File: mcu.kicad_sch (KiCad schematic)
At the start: 49 parts, among them J1 JTAG, J4 BOOT0, J5 Debug, SW1 ~{RST}, SW2 Config, U1 STM32H573VITx, U10 IS66WVS8M8FBLL-104NL, Y1 25MHz

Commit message: drawings: added title and project name
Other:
- company: (none) -> github.com/gabbla
- title: (none) -> MCU
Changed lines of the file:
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@@
 	(generator_version "8.0")
 	(paper "A3")
+	(title_block
+		(title "MCU")
+		(rev "v0.1.0")
+		(company "github.com/gabbla")
+		(comment 1 "${PROJECTNAME}")
+	)

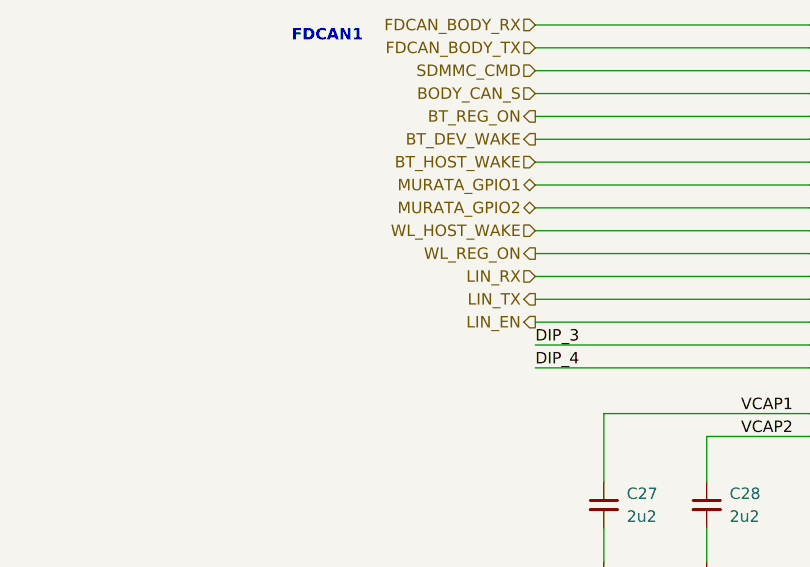
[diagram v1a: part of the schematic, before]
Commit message: sch: added UART4 note on LIN
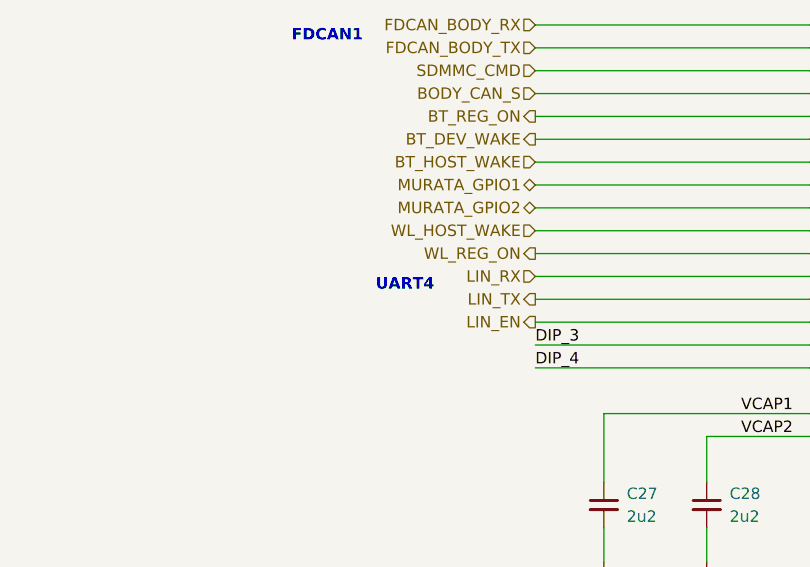
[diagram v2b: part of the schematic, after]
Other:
- note added: "UART4"

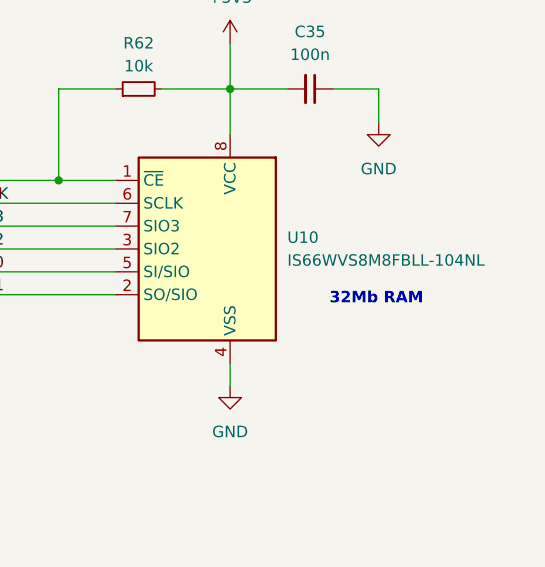
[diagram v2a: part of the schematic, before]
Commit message: External RAM changed to APS6404L 64Mbit
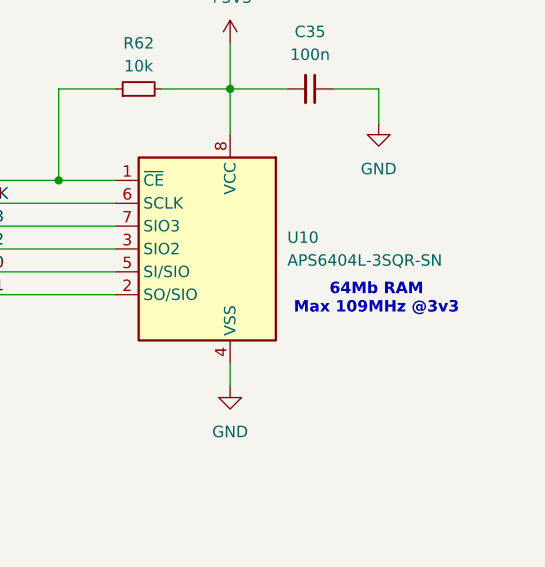
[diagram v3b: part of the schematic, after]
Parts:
- U10: value IS66WVS8M8FBLL-104NL -> APS6404L-3SQR-SN
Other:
- note added: "64Mb RAM Max 109MHz @3v3"
- note removed: "32Mb RAM"

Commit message: io, spi flash, stuff
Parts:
- added C24, C25: 100n, Capacitor_SMD:C_0603_1608Metric_Pad1.08x0.95mm_HandSolder, symbol Device:C_Small
- added R25, R26, R27: 4k7, Resistor_SMD:R_0603_1608Metric_Pad0.98x0.95mm_HandSolder, symbol Device:R_Small
- added R28: 10k, Resistor_SMD:R_0603_1608Metric_Pad0.98x0.95mm_HandSolder, symbol Device:R_Small
- added U3: PCA9557PW, Package_SO:TSSOP-16_4.4x5mm_P0.65mm, symbol Interface_Expansion:PCA9557PW
- added U4: SST25VF080B-50-4x-S2Ax, Package_SO:SOIC-8_5.275x5.275mm_P1.27mm, symbol Memory_Flash:SST25VF080B-50-4x-S2Ax
- renumbered C3 to C11, C11 to C12, C2 to C13, C12 to C14, C27 to C15, C28 to C16, C1 to C17, C29 to C18, C30 to C19, C31 to C20, C32 to C21, C33 to C22, C34 to C23, C35 to C26, D9 to D10, D10 to D11, D11 to D12, D1 to D5, D5 to D6, D6 to D7, D7 to D8, D8 to D9, J4 to J2, J1 to J3, J5 to J4, R1 to R15, R4 to R16, R38 to R17, R39 to R18, R40 to R19, R41 to R20, R5 to R21, R35 to R22, R36 to R23, R37 to R24, R62 to R29, R23 to R30, R24 to R31, R25 to R32, R26 to R33, R27 to R34, R28 to R35, R29 to R36, R30 to R37, U1 to U2, U10 to U5
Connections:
- net +3V3: now also C24.2, C25.2, R25.1, R26.1, R27.1, R28.2, U3.16 (VDD), U4.8 (VDD)
- net DBG_UART_RX: now also U2.56 (PD9); no longer U2.54 (PB15)
- net DBG_UART_TX: now also J4.5 (Pin_5), U2.55 (PD8); no longer J4.3 (Pin_3), U2.53 (PB14)
- net GND: now also C24.1, C25.1, U3.3 (A0), U3.4 (A1), U3.5 (A2), U3.8 (VSS), U4.4 (VSS)
- net LED0: now also U3.13 (IO6); no longer U2.2 (PE3)
- net LED1: now also U3.14 (IO7); no longer U2.1 (PE2)
- net LED_BODY_ERR: now also U3.9 (IO2); no longer U2.97 (PE0)
- net LED_BODY_RX: now also U3.7 (IO1); no longer U2.96 (PB9)
- net LED_BODY_TX: now also U3.6 (IO0); no longer U2.95 (PB8)
- net LED_HLDX_ERR: now also U3.12 (IO5); no longer U2.3 (PE4)
- net LED_HLDX_RX: now also U3.11 (IO4); no longer U2.4 (PE5)
- net LED_HLDX_TX: now also U3.10 (IO3); no longer U2.5 (PE6)
- net MURATA_GPIO2: now also U2.18 (PC3); no longer U2.55 (PD8)
- net WL_HOST_WAKE: now also U2.54 (PB15); no longer U2.56 (PD9)
- net MCU_USER_INPUT_1: now reaches U2.45 (PE14)
- net MCU_USER_INPUT_2: now reaches U2.46 (PE15)
- net DBG_UART_CTS: now reaches U2.52 (PB13)
- net DBG_UART_CTS: now also J4.6 (Pin_6)
- net MCU_USER_OUTPUT_1: now reaches U2.8 (PC14)
- net MCU_USER_OUTPUT_2: now reaches U2.9 (PC15)
- net DBG_UART_RTS: now reaches J4.2 (Pin_2)
- net DBG_UART_RTS: now also U2.53 (PB14)
- new net: R27.2, U3.15 (~{RESET})
- new net I2C1_SCL: R25.2, U2.95 (PB8), U3.1 (SCL)
- new net I2C1_SDA: R26.2, U2.96 (PB9), U3.2 (SDA)
- new net SPI4_MISO: U2.4 (PE5), U4.2 (SO)
- new net SPI4_MOSI: U2.5 (PE6), U4.5 (SI)
- new net SPI4_SCK: U2.1 (PE2), U4.6 (SCK)
- new net SPI4_~{CS}: R28.1, U2.3 (PE4), U4.1 (~{CE})
- no-connect marks 13 -> 9
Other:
- note added: "USART3"
- note removed: "USART1"
- moved on the sheet: C11, C12, C14, C15, C16, C18, C19, C20, C21, C22, C23, C26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
